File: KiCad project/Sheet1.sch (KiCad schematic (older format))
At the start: 28 parts, among them CON1 USB-MICRO-B, U1 EFM32GG332, U2 BQ25011

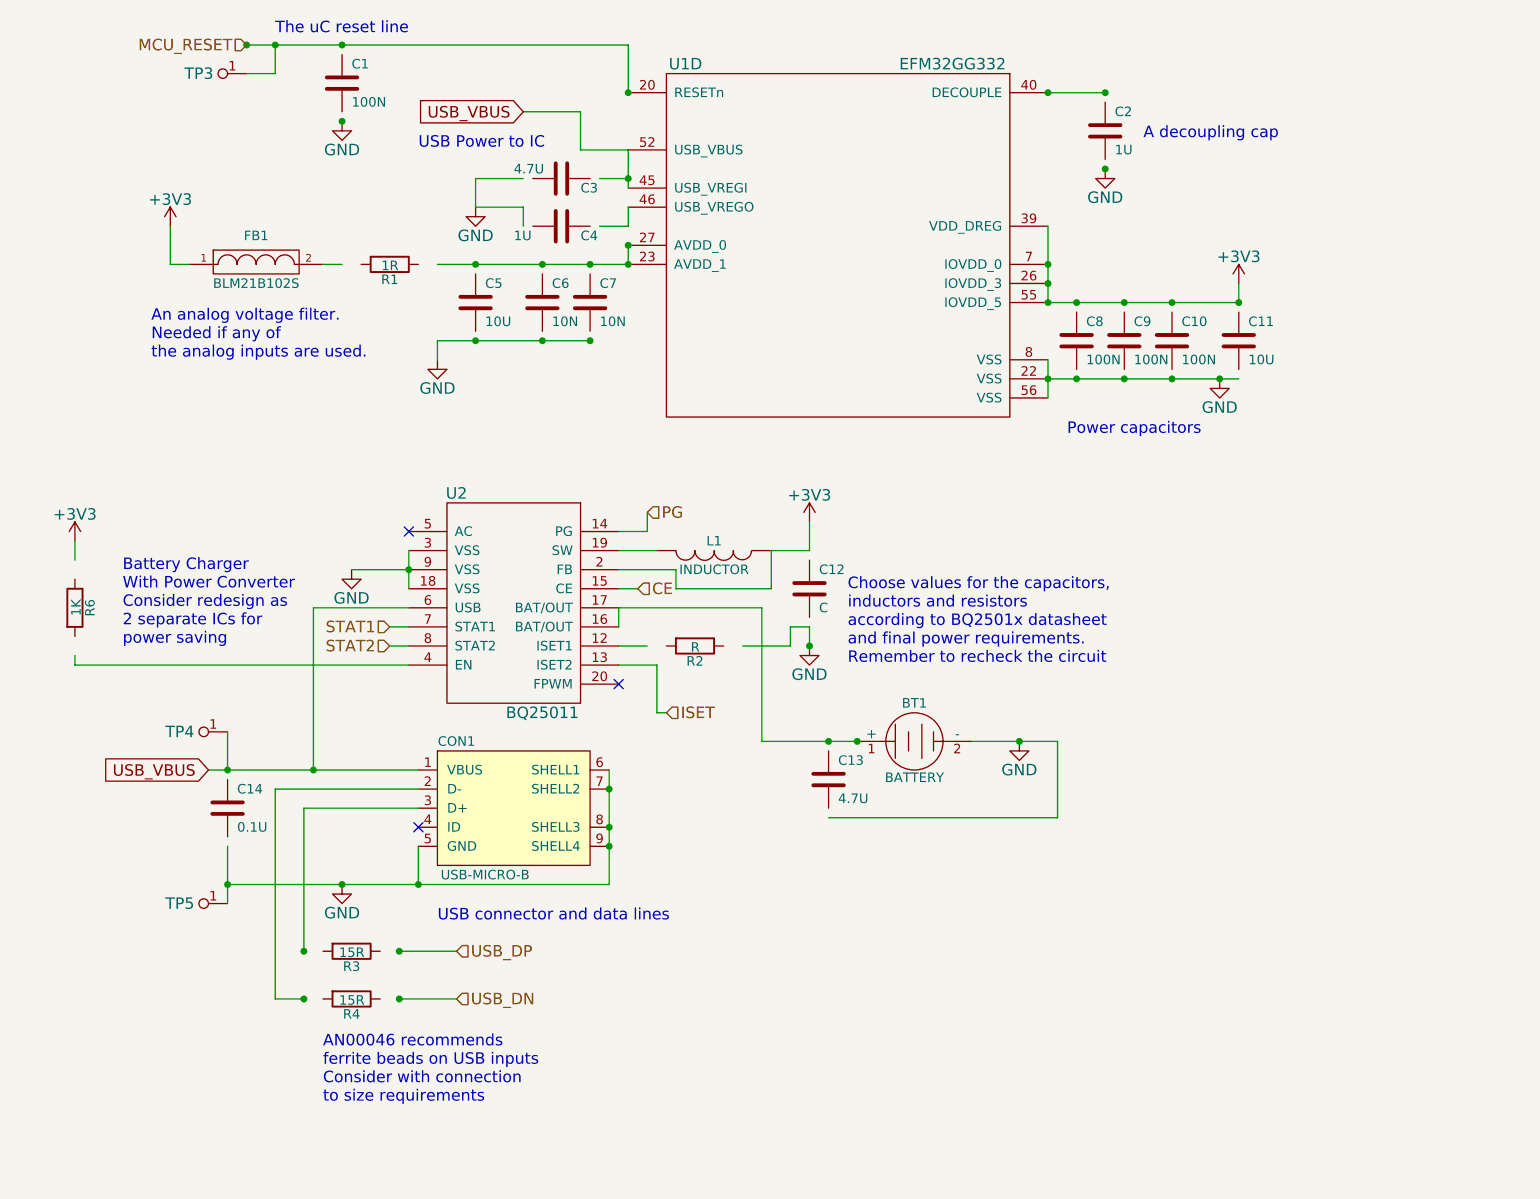
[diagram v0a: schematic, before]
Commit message: IC packages, bugfixes
drawings for IC packages, associations, schematic fixes
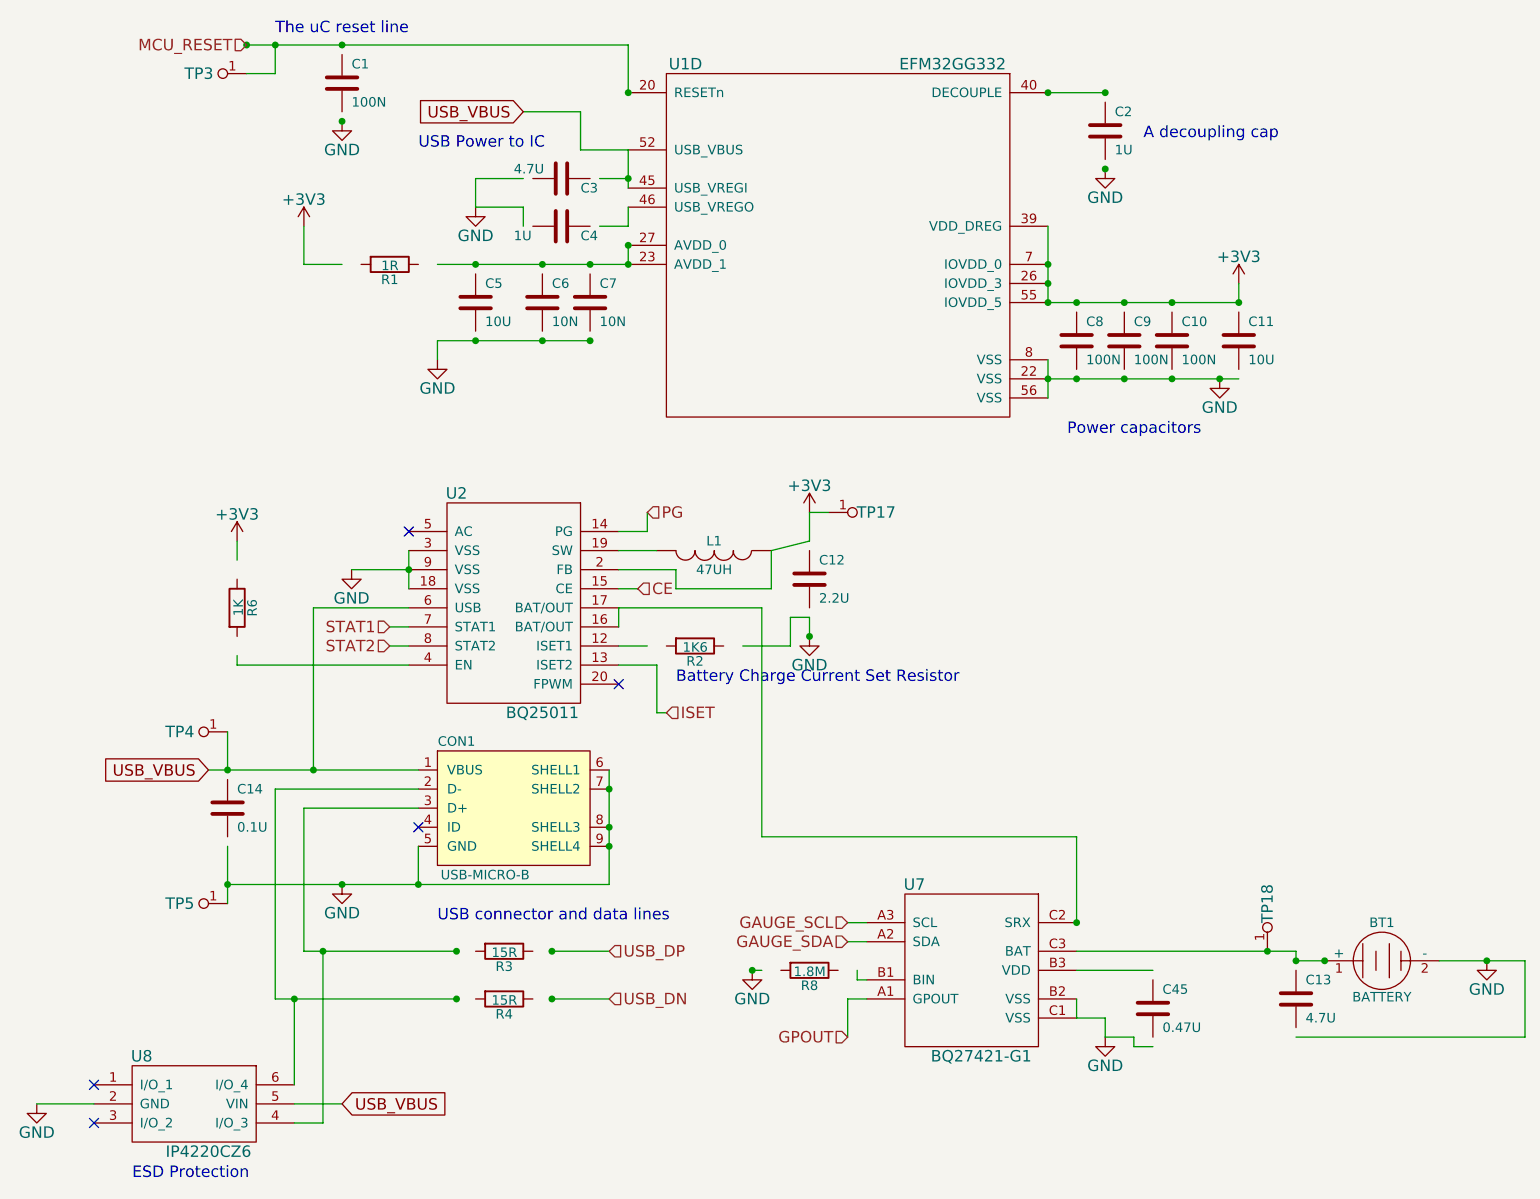
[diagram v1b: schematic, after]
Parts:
- removed FB1: BLM21B102S, symbol FILTER
- added C45: 0.47U, symbol C
- added R8: 1.8M, symbol R
- added TP17, TP18: TESTPAD, symbol TESTPAD
- added U7: BQ27421-G1, Anastasia:DSBGA9, symbol BQ27421-G1
- added U8: IP4220CZ6, Anastasia:SOT457, symbol IP4220CZ6
- C12: value C -> 2.2U
- CON1: footprint (none) -> Connect:USB_Micro-B
- L1: value INDUCTOR -> 47UH
- R2: value R -> 1K6
- U1: footprint (none) -> Housings_QFP:TQFP-64_10x10mm_Pitch0.5mm
- U2: footprint (none) -> Anastasia:VQFN20
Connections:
- net labels added: GAUGE_SCL, GAUGE_SDA, GPOUT
- wire segments 75 -> 99
- no-connect marks 3 -> 5
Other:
- note added: "Battery Charge Current Set Resistor"
- note added: "ESD Protection\n"
- note removed: "AN00046 recommends \nferrite beads on USB inputs\nConsider with connection\nto size requirements"
- note removed: "An analog voltage filter. \nNeeded if any of \nthe analog inputs are used.\n"
- note removed: "Battery Charger\nWith Power Converter\nConsider redesign as \n2 separate ICs for\npower saving"
- note removed: "Choose values for the capacitors,\ninductors and resistors\naccording to BQ2501x datasheet\nand final power requirements.\nRemember to recheck the circuit"
- moved on the sheet: BT1, C12, C13, R3, R4, R6

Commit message: New packages, PCB
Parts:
- BT1: footprint (none) -> Anastasia:BATTERY
- C1, C10, C11, C12, C2, C3, C4, C5, C6, C7, C8, C9: footprint (none) -> Capacitors_SMD:C_0603
- C13: renamed from C14; footprint (none) -> Capacitors_SMD:C_0603
- C14: renamed from C13; footprint (none) -> Capacitors_SMD:C_0603
- C15: renamed from C45; footprint (none) -> Capacitors_SMD:C_0603
- L1, R1: footprint (none) -> Resistors_SMD:R_0603
- R2: renamed from R6; footprint (none) -> Resistors_SMD:R_0603
- R3: renamed from R2; footprint (none) -> Resistors_SMD:R_0603
- R4: renamed from R3; footprint (none) -> Resistors_SMD:R_0603
- R5: renamed from R8; footprint (none) -> Resistors_SMD:R_0603
- R6: renamed from R4; footprint (none) -> Resistors_SMD:R_0603
- TP12: renamed from TP3; footprint (none) -> Measurement_Points:Measurement_Point_Round-SMD-Pad_Small
- TP13: renamed from TP17; footprint (none) -> Measurement_Points:Measurement_Point_Round-SMD-Pad_Small
- TP14: renamed from TP4; footprint (none) -> Measurement_Points:Measurement_Point_Round-SMD-Pad_Small
- TP15: renamed from TP5; footprint (none) -> Measurement_Points:Measurement_Point_Round-SMD-Pad_Small
- TP16: renamed from TP18; footprint (none) -> Measurement_Points:Measurement_Point_Round-SMD-Pad_Small
- renumbered U7 to U3, U8 to U4
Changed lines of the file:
@@
 F 0 "C1" H 2300 1300 50  0000 L CNN
 F 1 "100N" H 2300 1100 50  0000 L CNN
-F 2 "" H 2288 1050 30  0001 C CNN
+F 2 "Capacitors_SMD:C_0603" H 2288 1050 30  0001 C CNN
 F 3 "" H 2250 1200 60  0000 C CNN
 	1    2250 1200
@@
 F 0 "R1" V 2580 2150 50  0000 C CNN
 F 1 "1R" V 2507 2151 50  0000 C CNN
-F 2 "" V 2430 2150 30  0001 C CNN
+F 2 "Resistors_SMD:R_0603" V 2430 2150 30  0001 C CNN
 F 3 "" H 2500 2150 30  0000 C CNN
 	1    2500 2150
@@
 F 0 "C5" H 3000 2450 50  0000 L CNN
 F 1 "10U" H 3000 2250 50  0000 L CNN
-F 2 "" H 2988 2200 30  0001 C CNN
+F 2 "Capacitors_SMD:C_0603" H 2988 2200 30  0001 C CNN
 F 3 "" H 2950 2350 60  0000 C CNN
 	1    2950 2350
@@
 F 0 "C6" H 3350 2450 50  0000 L CNN
 F 1 "10N" H 3350 2250 50  0000 L CNN
-F 2 "" H 3338 2200 30  0001 C CNN
+F 2 "Capacitors_SMD:C_0603" H 3338 2200 30  0001 C CNN
 F 3 "" H 3300 2350 60  0000 C CNN
 	1    3300 2350
@@
 F 0 "C7" H 3600 2450 50  0000 L CNN
 F 1 "10N" H 3600 2250 50  0000 L CNN
-F 2 "" H 3588 2200 30  0001 C CNN
+F 2 "Capacitors_SMD:C_0603" H 3588 2200 30  0001 C CNN
 F 3 "" H 3550 2350 60  0000 C CNN
 	1    3550 2350
@@
 F 0 "C2" H 6300 1550 50  0000 L CNN
 F 1 "1U" H 6300 1350 50  0000 L CNN
-F 2 "" H 6288 1300 30  0001 C CNN
+F 2 "Capacitors_SMD:C_0603" H 6288 1300 30  0001 C CNN
 F 3 "" H 6250 1450 60  0000 C CNN
 	1    6250 1450
@@
 F 0 "C8" H 6150 2650 50  0000 L CNN
 F 1 "100N" H 6150 2450 50  0000 L CNN
-F 2 "" H 6138 2400 30  0001 C CNN
+F 2 "Capacitors_SMD:C_0603" H 6138 2400 30  0001 C CNN
 F 3 "" H 6100 2550 60  0000 C CNN
 	1    6100 2550
@@
 F 0 "C9" H 6400 2650 50  0000 L CNN
 F 1 "100N" H 6400 2450 50  0000 L CNN
-F 2 "" H 6388 2400 30  0001 C CNN
+F 2 "Capacitors_SMD:C_0603" H 6388 2400 30  0001 C CNN
 F 3 "" H 6350 2550 60  0000 C CNN
 	1    6350 2550
@@
 F 0 "C10" H 6650 2650 50  0000 L CNN
 F 1 "100N" H 6650 2450 50  0000 L CNN
-F 2 "" H 6638 2400 30  0001 C CNN
+F 2 "Capacitors_SMD:C_0603" H 6638 2400 30  0001 C CNN
 F 3 "" H 6600 2550 60  0000 C CNN
 	1    6600 2550
@@
 F 0 "C11" H 7000 2650 50  0000 L CNN
 F 1 "10U" H 7000 2450 50  0000 L CNN
-F 2 "" H 6988 2400 30  0001 C CNN
+F 2 "Capacitors_SMD:C_0603" H 6988 2400 30  0001 C CNN
 F 3 "" H 6950 2550 60  0000 C CNN
 	1    6950 2550
@@
 $EndComp
 $Comp
-L C C14
+L C C13
 U 1 1 550474F1
 P 1650 5000
-F 0 "C14" H 1700 5100 50  0000 L CNN
+F 0 "C13" H 1700 5100 50  0000 L CNN
 F 1 "0.1U" H 1700 4900 50  0000 L CNN
-F 2 "" H 1688 4850 30  0001 C CNN
+F 2 "Capacitors_SMD:C_0603" H 1688 4850 30  0001 C CNN
 F 3 "" H 1650 5000 60  0000 C CNN
 	1    1650 5000
@@
 F 0 "L1" V 4150 3650 50  0000 C CNN
 F 1 "47UH" V 4300 3650 50  0000 C CNN
-F 2 "" H 4200 3650 60  0001 C CNN
+F 2 "Resistors_SMD:R_0603" H 4200 3650 60  0001 C CNN
 F 3 "" H 4200 3650 60  0000 C CNN
 	1    4200 3650
@@
 F 0 "C12" H 4750 3900 50  0000 L CNN
 F 1 "2.2U" H 4750 3700 50  0000 L CNN
-F 2 "" H 4738 3650 30  0001 C CNN
+F 2 "Capacitors_SMD:C_0603" H 4738 3650 30  0001 C CNN
 F 3 "" H 4700 3800 60  0000 C CNN
 	1    4700 3800
@@
 $EndComp
 $Comp
-L R R2
+L R R3
 U 1 1 55047512
 P 4100 4150
-F 0 "R2" V 4180 4150 50  0000 C CNN
+F 0 "R3" V 4180 4150 50  0000 C CNN
 F 1 "1K6" V 4107 4151 50  0000 C CNN
-F 2 "" V 4030 4150 30  0001 C CNN
+F 2 "Resistors_SMD:R_0603" V 4030 4150 30  0001 C CNN
 F 3 "" H 4100 4150 30  0000 C CNN
 	1    4100 4150
@@
 F 0 "C3" V 3450 1800 50  0000 L CNN
 F 1 "4.7U" V 3350 1450 50  0000 L CNN
-F 2 "" H 3438 1550 30  0001 C CNN
+F 2 "Capacitors_SMD:C_0603" H 3438 1550 30  0001 C CNN
 F 3 "" H 3400 1700 60  0000 C CNN
 	1    3400 1700
@@
 F 0 "C4" V 3450 2050 50  0000 L CNN
 F 1 "1U" V 3450 1700 50  0000 L CNN
-F 2 "" H 3438 1800 30  0001 C CNN
+F 2 "Capacitors_SMD:C_0603" H 3438 1800 30  0001 C CNN
 F 3 "" H 3400 1950 60  0000 C CNN
 	1    3400 1950
@@
 $EndComp
 $Comp
-L R R3
+L R R4
 U 1 1 55047530
 P 3100 5750
-F 0 "R3" V 3180 5750 50  0000 C CNN
+F 0 "R4" V 3180 5750 50  0000 C CNN
 F 1 "15R" V 3107 5751 50  0000 C CNN
-F 2 "" V 3030 5750 30  0001 C CNN
+F 2 "Resistors_SMD:R_0603" V 3030 5750 30  0001 C CNN
 F 3 "" H 3100 5750 30  0000 C CNN
 	1    3100 5750
@@
 $EndComp
 $Comp
-L R R4
+L R R6
 U 1 1 55047537
 P 3100 6000
-F 0 "R4" V 3180 6000 50  0000 C CNN
+F 0 "R6" V 3180 6000 50  0000 C CNN
 F 1 "15R" V 3107 6001 50  0000 C CNN
-F 2 "" V 3030 6000 30  0001 C CNN
+F 2 "Resistors_SMD:R_0603" V 3030 6000 30  0001 C CNN
 F 3 "" H 3100 6000 30  0000 C CNN
 	1    3100 6000
@@
 F 0 "BT1" H 7700 6000 50  0000 C CNN
 F 1 "BATTERY" H 7700 5610 50  0000 C CNN
-F 2 "" H 7700 5800 60  0001 C CNN
+F 2 "Anastasia:BATTERY" H 7700 5800 60  0001 C CNN
 F 3 "" H 7700 5800 60  0000 C CNN
 	1    7700 5800
@@
 $EndComp
 $Comp
-L C C13
+L C C14
 U 1 1 550479A6
 P 7250 6000
-F 0 "C13" H 7300 6100 50  0000 L CNN
+F 0 "C14" H 7300 6100 50  0000 L CNN
 F 1 "4.7U" H 7300 5900 50  0000 L CNN
-F 2 "" H 7288 5850 30  0001 C CNN
+F 2 "Capacitors_SMD:C_0603" H 7288 5850 30  0001 C CNN
 F 3 "" H 7250 6000 60  0000 C CNN
 	1    7250 6000
@@
 MCU_RESET
 $Comp
-L TESTPAD TP3
+L TESTPAD TP12
 U 1 1 5506D7F2
 P 1750 1150
-F 0 "TP3" H 2000 1150 60  0000 C CNN
+F 0 "TP12" H 2000 1150 60  0000 C CNN
 F 1 "TESTPAD" H 1800 950 60  0001 C CNN
-F 2 "" H 2000 1150 60  0001 C CNN
+F 2 "Measurement_Points:Measurement_Point_Round-SMD-Pad_Small" H 2000 1150 60  0001 C CNN
 F 3 "" H 2000 1150 60  0000 C CNN
 	1    1750 1150
@@
 STAT2
 $Comp
-L R R6
+L R R2
 U 1 1 5507251D
 P 1700 3950
-F 0 "R6" V 1780 3950 50  0000 C CNN
+F 0 "R2" V 1780 3950 50  0000 C CNN
 F 1 "1K" V 1707 3951 50  0000 C CNN
-F 2 "" V 1630 3950 30  0001 C CNN
+F 2 "Resistors_SMD:R_0603" V 1630 3950 30  0001 C CNN
 F 3 "" H 1700 3950 30  0000 C CNN
 	1    1700 3950
@@
 $EndComp
 $Comp
-L TESTPAD TP4
+L TESTPAD TP14
 U 1 1 55072D4F
 P 1650 4600
-F 0 "TP4" H 1900 4600 60  0000 C CNN
+F 0 "TP14" H 1900 4600 60  0000 C CNN
 F 1 "TESTPAD" H 1700 4400 60  0001 C CNN
-F 2 "" H 1900 4600 60  0001 C CNN
+F 2 "Measurement_Points:Measurement_Point_Round-SMD-Pad_Small" H 1900 4600 60  0001 C CNN
 F 3 "" H 1900 4600 60  0000 C CNN
 	1    1650 4600
@@
 $EndComp
 $Comp
-L TESTPAD TP5
+L TESTPAD TP15
 U 1 1 550731F6
 P 1650 5500
-F 0 "TP5" H 1900 5500 60  0000 C CNN
+F 0 "TP15" H 1900 5500 60  0000 C CNN
 F 1 "TESTPAD" H 1700 5300 60  0001 C CNN
-F 2 "" H 1900 5500 60  0001 C CNN
+F 2 "Measurement_Points:Measurement_Point_Round-SMD-Pad_Small" H 1900 5500 60  0001 C CNN
 F 3 "" H 1900 5500 60  0000 C CNN
 	1    1650 5500
@@
 CE
 $Comp
-L BQ27421-G1 U7
+L BQ27421-G1 U3
 U 1 1 550850D9
 P 5200 5450
-F 0 "U7" H 5250 5500 60  0000 C CNN
+F 0 "U3" H 5250 5500 60  0000 C CNN
 F 1 "BQ27421-G1" H 5600 4600 60  0000 C CNN
 F 2 "Anastasia:DSBGA9" H 5200 5450 60  0001 C CNN
@@
 $EndComp
 $Comp
-L C C45
+L C C15
 U 1 1 55085D1A
 P 6500 6050
-F 0 "C45" H 6550 6150 50  0000 L CNN
+F 0 "C15" H 6550 6150 50  0000 L CNN
 F 1 "0.47U" H 6550 5950 50  0000 L CNN
-F 2 "" H 6538 5900 30  0001 C CNN
+F 2 "Capacitors_SMD:C_0603" H 6538 5900 30  0001 C CNN
 F 3 "" H 6500 6050 60  0000 C CNN
 	1    6500 6050
@@
 $EndComp
 $Comp
-L R R8
+L R R5
 U 1 1 5508617A
 P 4700 5850
-F 0 "R8" V 4780 5850 50  0000 C CNN
+F 0 "R5" V 4780 5850 50  0000 C CNN
 F 1 "1.8M" V 4707 5851 50  0000 C CNN
-F 2 "" V 4630 5850 30  0001 C CNN
+F 2 "Resistors_SMD:R_0603" V 4630 5850 30  0001 C CNN
 F 3 "" H 4700 5850 30  0000 C CNN
 	1    4700 5850
@@
 	4900 6000 5000 6000
 $Comp
-L IP4220CZ6 U8
+L IP4220CZ6 U4
 U 1 1 55094F19
 P 1150 6350
-F 0 "U8" H 1200 6400 60  0000 C CNN
+F 0 "U4" H 1200 6400 60  0000 C CNN
 F 1 "IP4220CZ6" H 1550 5900 60  0000 C CNN
 F 2 "Anastasia:SOT457" H 1150 6350 60  0001 C CNN
@@
 	6100 5150 6100 5600
 $Comp
-L TESTPAD TP18
+L TESTPAD TP16
 U 1 1 550C93EA
 P 7100 5750
-F 0 "TP18" H 7350 5750 60  0000 C CNN
+F 0 "TP16" H 7350 5750 60  0000 C CNN
 F 1 "TESTPAD" H 7150 5550 60  0001 C CNN
-F 2 "" H 7350 5750 60  0000 C CNN
+F 2 "Measurement_Points:Measurement_Point_Round-SMD-Pad_Small" H 7350 5750 60  0001 C CNN
 F 3 "" H 7350 5750 60  0000 C CNN
 	1    7100 5750
@@
 $EndComp
 $Comp
-L TESTPAD TP17
+L TESTPAD TP13
 U 1 1 550CAB5D
 P 4800 3450
-F 0 "TP17" H 5050 3450 60  0000 C CNN
+F 0 "TP13" H 5050 3450 60  0000 C CNN
 F 1 "TESTPAD" H 4850 3250 60  0001 C CNN
-F 2 "" H 5050 3450 60  0000 C CNN
+F 2 "Measurement_Points:Measurement_Point_Round-SMD-Pad_Small" H 5050 3450 60  0001 C CNN
 F 3 "" H 5050 3450 60  0000 C CNN
 	1    4800 3450

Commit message: PCB design
Routing for the main components, except for the power section
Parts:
- TP12, TP13, TP14, TP15, TP16: footprint Measurement_Points:Measurement_Point_Round-SMD-Pad_Small -> Anastasia:Test_Point_Round-SMD-Pad
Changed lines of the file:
@@
 F 0 "TP12" H 2000 1150 60  0000 C CNN
 F 1 "TESTPAD" H 1800 950 60  0001 C CNN
-F 2 "Measurement_Points:Measurement_Point_Round-SMD-Pad_Small" H 2000 1150 60  0001 C CNN
+F 2 "Anastasia:Test_Point_Round-SMD-Pad" H 2000 1150 60  0001 C CNN
 F 3 "" H 2000 1150 60  0000 C CNN
 	1    1750 1150
@@
 F 0 "TP14" H 1900 4600 60  0000 C CNN
 F 1 "TESTPAD" H 1700 4400 60  0001 C CNN
-F 2 "Measurement_Points:Measurement_Point_Round-SMD-Pad_Small" H 1900 4600 60  0001 C CNN
+F 2 "Anastasia:Test_Point_Round-SMD-Pad" H 1900 4600 60  0001 C CNN
 F 3 "" H 1900 4600 60  0000 C CNN
 	1    1650 4600
@@
 F 0 "TP15" H 1900 5500 60  0000 C CNN
 F 1 "TESTPAD" H 1700 5300 60  0001 C CNN
-F 2 "Measurement_Points:Measurement_Point_Round-SMD-Pad_Small" H 1900 5500 60  0001 C CNN
+F 2 "Anastasia:Test_Point_Round-SMD-Pad" H 1900 5500 60  0001 C CNN
 F 3 "" H 1900 5500 60  0000 C CNN
 	1    1650 5500
@@
 F 0 "TP16" H 7350 5750 60  0000 C CNN
 F 1 "TESTPAD" H 7150 5550 60  0001 C CNN
-F 2 "Measurement_Points:Measurement_Point_Round-SMD-Pad_Small" H 7350 5750 60  0001 C CNN
+F 2 "Anastasia:Test_Point_Round-SMD-Pad" H 7350 5750 60  0001 C CNN
 F 3 "" H 7350 5750 60  0000 C CNN
 	1    7100 5750
@@
 F 0 "TP13" H 5050 3450 60  0000 C CNN
 F 1 "TESTPAD" H 4850 3250 60  0001 C CNN
-F 2 "Measurement_Points:Measurement_Point_Round-SMD-Pad_Small" H 5050 3450 60  0001 C CNN
+F 2 "Anastasia:Test_Point_Round-SMD-Pad" H 5050 3450 60  0001 C CNN
 F 3 "" H 5050 3450 60  0000 C CNN
 	1    4800 3450
